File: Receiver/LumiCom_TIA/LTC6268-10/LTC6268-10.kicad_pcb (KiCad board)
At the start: 4 copper layers, 30 x 40 mm, 28 parts, among them J1 IN, J2 Vout, J3 TEST, J4 OUT, U1 LTC6268-10-SOT23

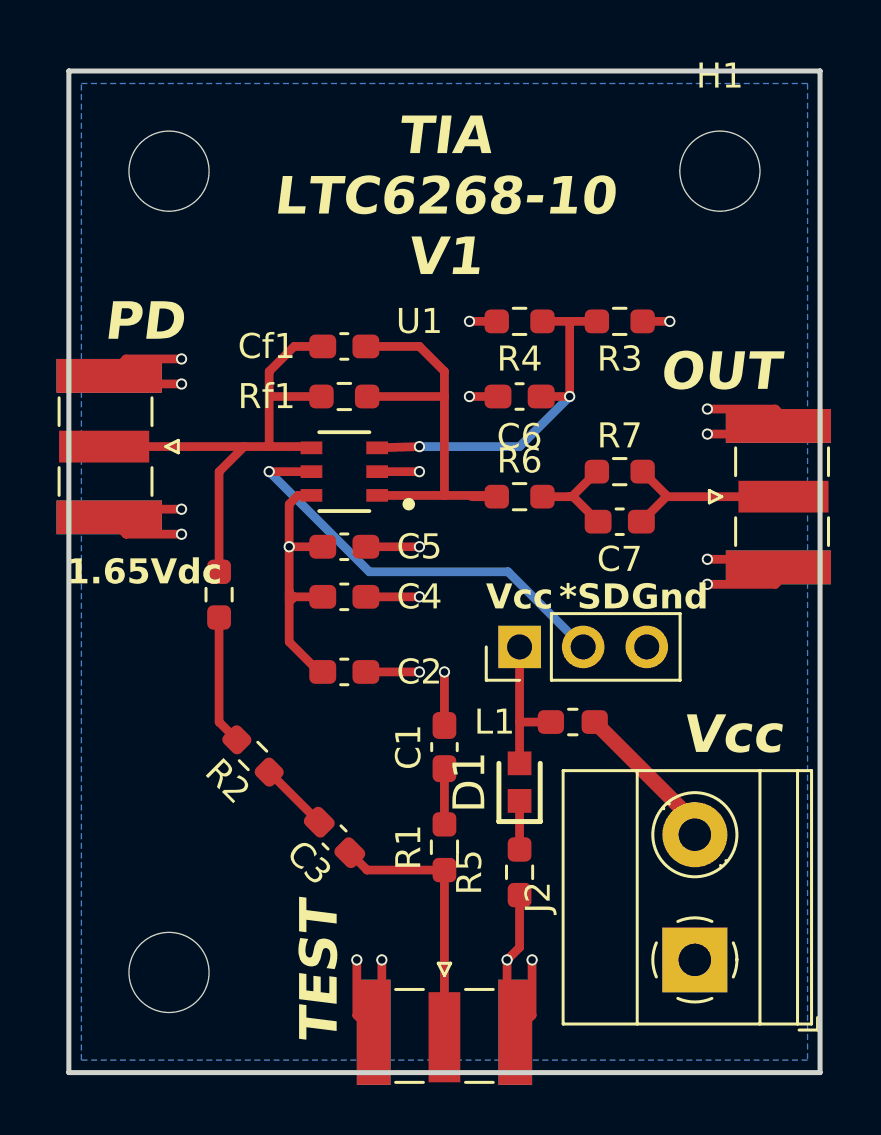
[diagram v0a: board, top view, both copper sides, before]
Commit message: Small updates
Update silkscreen font, height and weight
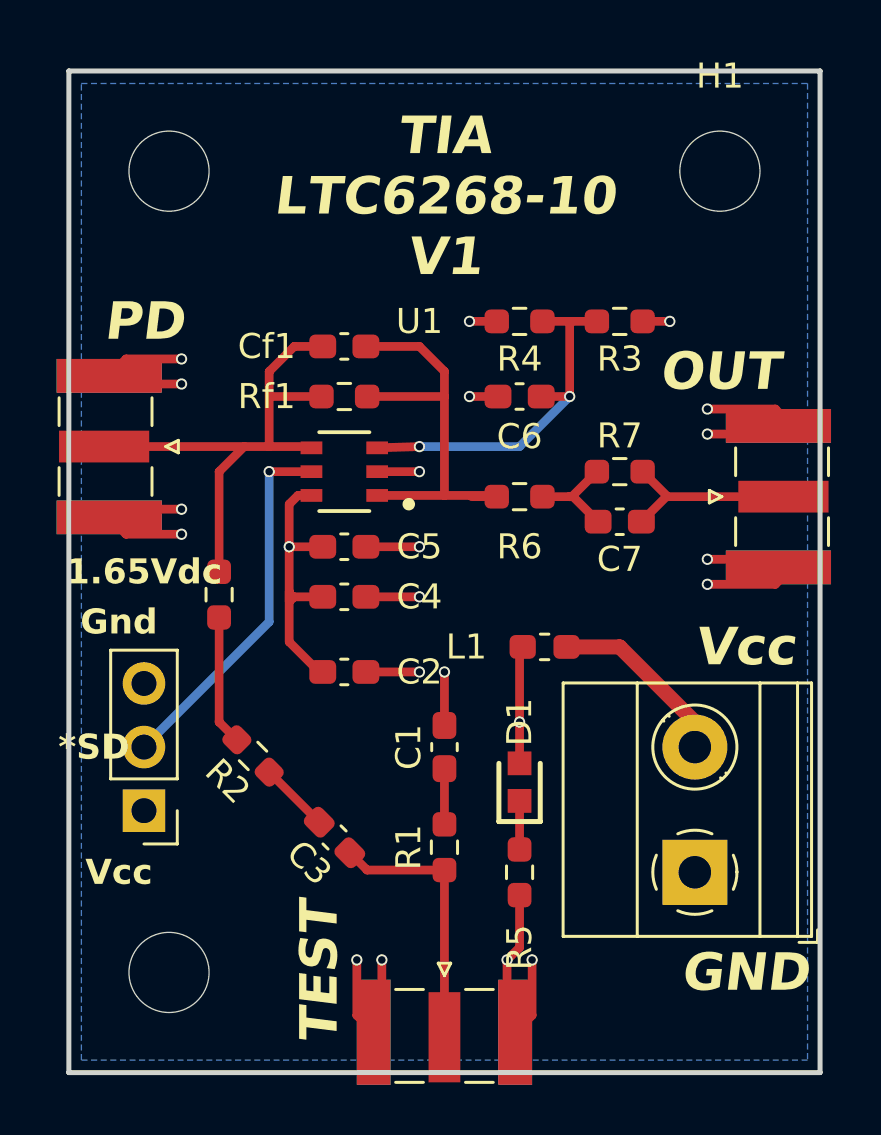
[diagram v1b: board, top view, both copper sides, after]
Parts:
- moved SD_L1 16.4 mm to (109.9, 82.5), turned to 180 degrees
- moved J2 3.50 mm to (131.9, 85.0)
- moved L1 3.20 mm to (125.9, 76.0)
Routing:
- net /Shutdown_L: track 17.1 -> 14.8 mm
- net Net-(J2-Pin_2): track 6.16 -> 7.37 mm
- net VCC: track 18.5 -> 17.3 mm, vias 2 -> 3
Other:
- board text added: "GND"
